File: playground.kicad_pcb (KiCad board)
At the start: 4 copper layers, 80 x 51 mm, 74 parts, among them IC1 TXU0101DBVR, IC11 LM3940IMP-3.3_NOPB, IC2 TXU0101DBVR, IC3 TXU0101DBVR, IC4 TXU0101DBVR, IC5 TXU0101DBVR, IC6 TXU0101DBVR, IC7 TXU0101DBVR, IC8 TXU0101DBVR, IC9 L293DD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

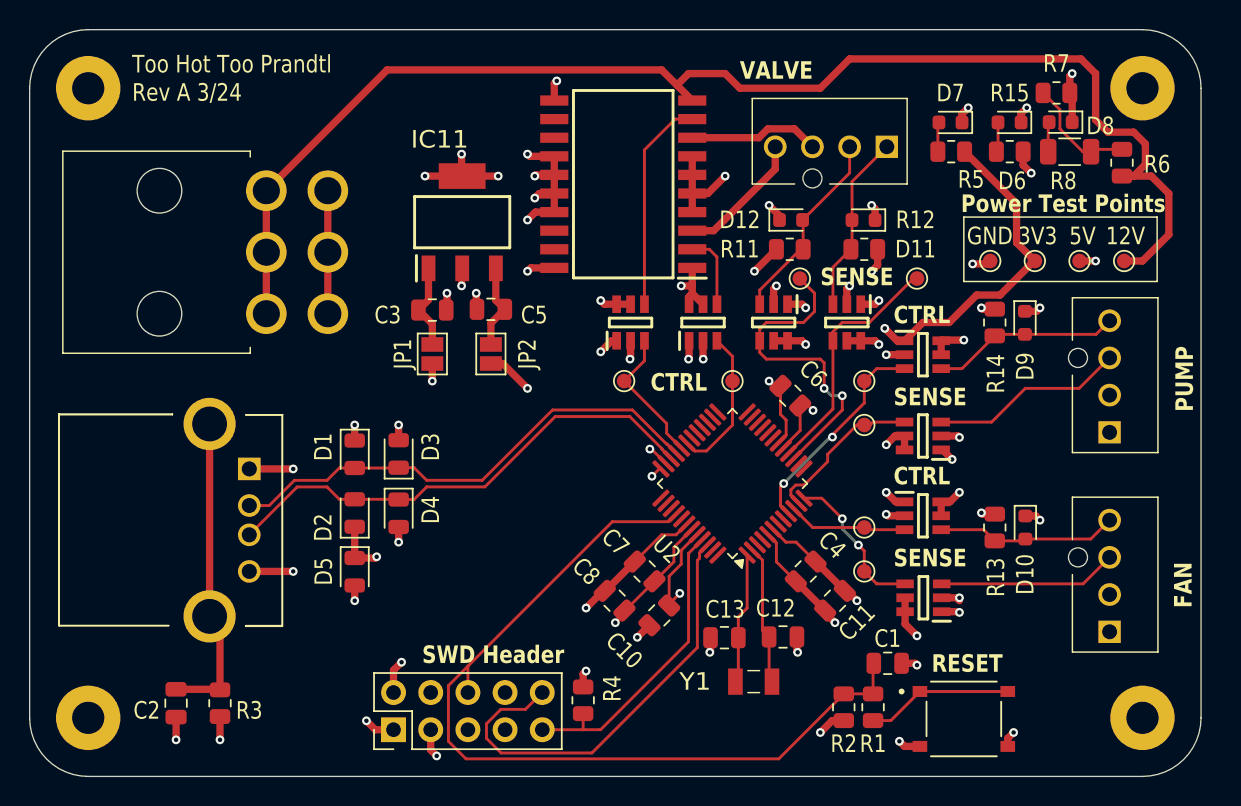
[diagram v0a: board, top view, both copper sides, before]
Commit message: Small part substitutions. Working on BOM
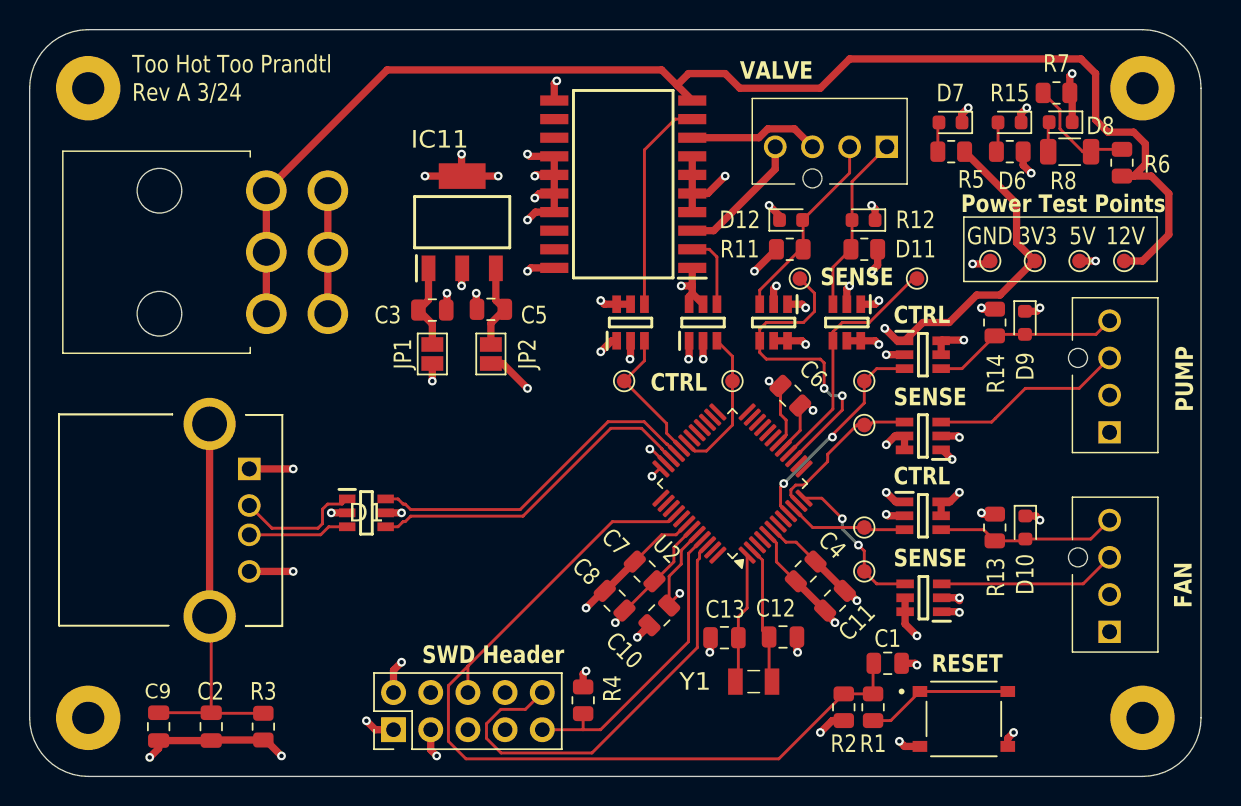
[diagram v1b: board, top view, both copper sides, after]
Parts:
- removed D2: D_Zener, Diode_SMD:D_0805_2012Metric
- removed D3, D4, D5: ~, Diode_SMD:D_0805_2012Metric
- added C9: 2.2n, Capacitor_SMD:C_0805_2012Metric, F.Cu at (90.8, 106.6)
- C2: value 4.5nF -> 2.2n
- C3: value 4.7n -> 470n
- D1: value ~ -> IP4234CZ6,125; footprint Diode_SMD:D_0805_2012Metric -> custom_footprints:SOP95P275X110-6N
- moved D1 4.08 mm to (105.0, 92.0), turned to 0 degrees
- moved R3 3.36 mm to (98.0, 106.6)
- moved C2 2.88 mm to (94.4, 106.6)
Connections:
- D1 pad 1: +5V -> /IN_USB_D-
- D1 pad 2: /USB_D- -> GND
- J1 pad 2: /USB_D- -> /IN_USB_D-
- J1 pad 3: /USB_D+ -> /IN_USB_D+
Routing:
- net /USB_D+: track 34.1 -> 23.2 mm
- net /USB_D-: track 33.9 -> 23.5 mm
- net /IN_USB_D-: track 0.00 -> 8.74 mm
- net /IN_USB_D+: track 0.00 -> 6.92 mm
- net /usb_shield_gnd: track 21.5 -> 28.2 mm
- net GND: track 97.9 -> 103.0 mm, vias 45 -> 43
- net +5V: track 37.1 -> 33.5 mm, vias 20 -> 19

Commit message: Added all part numbers
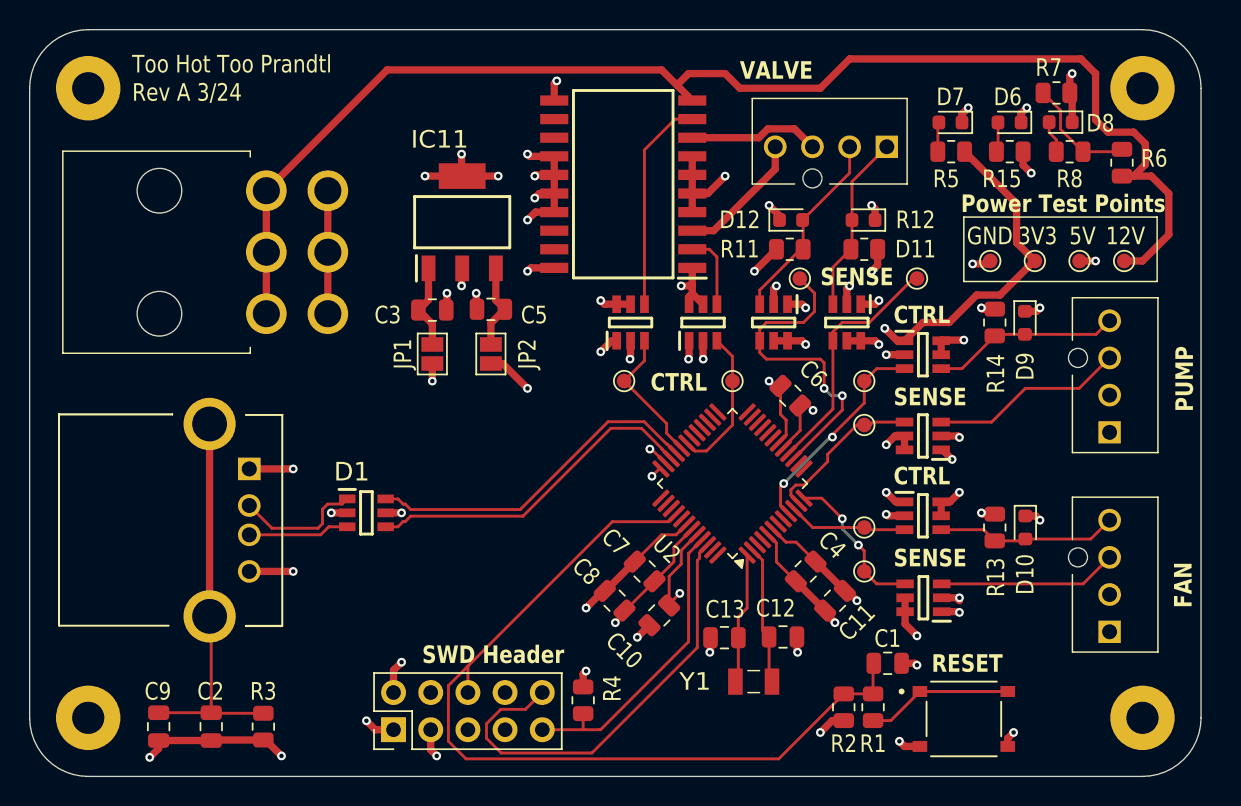
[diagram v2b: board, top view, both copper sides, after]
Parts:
- R11, R12, R13, R14, R15: value 20R -> 200R
- R8: footprint Resistor_SMD:R_1206_3216Metric -> Resistor_SMD:R_0805_2012Metric

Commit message: Version exported for production.
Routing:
- net +12V: track 93.2 -> 49.8 mm
- net GND: track 103.0 -> 94.6 mm
- added copper zone on F.Cu, net +12V
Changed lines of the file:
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@@
 	)
 	(segment
-		(start 117.828 63.84)
-		(end 117.828 62.672)
-		(width 0.5)
-		(layer "F.Cu")
-		(net 4)
-	)
-	(segment
 		(start 147.0875 92.0875)
 		(end 147 92)
@@
 	)
 	(segment
+		(start 117.788 63.8)
+		(end 117.828 63.84)
+		(width 0.5)
+		(layer "F.Cu")
+		(net 4)
+	)
+	(segment
 		(start 138.759466 77.75)
 		(end 139.75 77.75)
@@
 	)
 	(segment
-		(start 117.828 62.672)
-		(end 118 62.5)
-		(width 0.5)
-		(layer "F.Cu")
-		(net 4)
-	)
-	(segment
 		(start 133 74)
 		(end 131.5 75.5)
@@
 	)
 	(segment
+		(start 116 63.8)
+		(end 117.788 63.8)
+		(width 0.5)
+		(layer "F.Cu")
+		(net 4)
+	)
+	(segment
 		(start 144.25 87.7)
 		(end 144.35 87.7)
@@
 	)
 	(via
-		(at 118 62.5)
+		(at 116 63.8)
 		(size 0.6)
 		(drill 0.3)
@@
 	)
 	(segment
-		(start 102.364999 78.399999)
-		(end 102.365 74.199999)
-		(width 0.5)
-		(layer "F.Cu")
-		(net 5)
-	)
-	(segment
 		(start 127.252 70.19)
 		(end 128.31 70.19)
@@
 	)
 	(segment
-		(start 102.365 70)
-		(end 102.365 74.199999)
-		(width 0.5)
-		(layer "F.Cu")
-		(net 5)
-	)
-	(segment
 		(start 145.4 86.75)
 		(end 145.5 86.85)
@@
 	)
 	(segment
-		(start 138 61)
-		(end 153.8 61)
-		(width 0.5)
-		(layer "F.Cu")
-		(net 55)
-	)
-	(segment
-		(start 158.2 66.8)
-		(end 158.2 68.2)
-		(width 0.5)
-		(layer "F.Cu")
-		(net 55)
-	)
-	(segment
-		(start 125.162 61.75)
-		(end 126.206 62.794)
-		(width 0.5)
-		(layer "F.Cu")
-		(net 55)
-	)
-	(segment
-		(start 157.4 69)
-		(end 156.6 69)
-		(width 0.5)
-		(layer "F.Cu")
-		(net 55)
-	)
-	(segment
-		(start 154.8 65.159378)
-		(end 155.640622 66)
-		(width 0.5)
-		(layer "F.Cu")
-		(net 55)
-	)
-	(segment
-		(start 126.206 62.794)
-		(end 127.252 63.84)
-		(width 0.5)
-		(layer "F.Cu")
-		(net 55)
-	)
-	(segment
 		(start 159.8 73)
 		(end 159.8 70.2)
@@
 	)
 	(segment
-		(start 153.8 61)
-		(end 154.8 62)
-		(width 0.5)
-		(layer "F.Cu")
-		(net 55)
-	)
-	(segment
-		(start 158.2 68.2)
-		(end 157.4 69)
-		(width 0.5)
-		(layer "F.Cu")
-		(net 55)
-	)
-	(segment
-		(start 129.5 62)
-		(end 130.5 63)
-		(width 0.5)
-		(layer "F.Cu")
-		(net 55)
-	)
-	(segment
-		(start 154.8 62)
-		(end 154.8 65.159378)
-		(width 0.5)
-		(layer "F.Cu")
-		(net 55)
-	)
-	(segment
 		(start 156.75 74.8)
 		(end 158 74.8)
@@
 	)
 	(segment
-		(start 136 63)
-		(end 138 61)
-		(width 0.5)
-		(layer "F.Cu")
-		(net 55)
-	)
-	(segment
-		(start 127 62)
-		(end 129.5 62)
-		(width 0.5)
-		(layer "F.Cu")
-		(net 55)
-	)
-	(segment
-		(start 130.5 63)
-		(end 136 63)
+		(start 154.6 61.2)
+		(end 153.8 60.4)
 		(width 0.5)
 		(layer "F.Cu")
@@
 	)
 	(segment
-		(start 155.640622 66)
-		(end 157.4 66)
+		(start 155 66)
+		(end 154.6 65.6)
 		(width 0.5)
 		(layer "F.Cu")
@@
 	)
 	(segment
-		(start 157.4 66)
-		(end 158.2 66.8)
+		(start 157.8 66)
+		(end 155 66)
 		(width 0.5)
 		(layer "F.Cu")
@@
 	)
 	(segment
-		(start 98.165 69.999999)
-		(end 98.165 74.2)
+		(start 128.8 60.4)
+		(end 127.2 62)
 		(width 0.5)
 		(layer "F.Cu")
@@
 	)
 	(segment
-		(start 98.165 69.999999)
-		(end 106.414999 61.75)
+		(start 154.6 65.6)
+		(end 154.6 61.2)
 		(width 0.5)
 		(layer "F.Cu")
@@
 	)
 	(segment
-		(start 98.165 78.399999)
-		(end 98.165 74.2)
+		(start 158.6 69)
+		(end 158.6 66.8)
 		(width 0.5)
 		(layer "F.Cu")
@@
 	)
 	(segment
-		(start 126.206 62.794)
-		(end 127 62)
+		(start 153.8 60.4)
+		(end 128.8 60.4)
 		(width 0.5)
 		(layer "F.Cu")
@@
 	)
 	(segment
-		(start 106.414999 61.75)
-		(end 125.162 61.75)
+		(start 158.6 66.8)
+		(end 157.8 66)
 		(width 0.5)
 		(layer "F.Cu")
@@
 	)
 	(zone
+		(net 55)
+		(net_name "+12V")
+		(layer "F.Cu")
+		(hatch edge 0.5)
+		(priority 3)
+		(connect_pads yes
+			(clearance 0.5)
+		)
+		(min_thickness 0.25)
+		(filled_areas_thickness no)
+		(fill yes
+			(thermal_gap 0.5)
+			(thermal_bridge_width 0.5)
+		)
+		(polygon
+			(pts
+				(xy 100.2 68) (xy 100.2 80.2) (xy 96 80.2) (xy 96 68) (xy 101.6 62.4) (xy 105.6 62.4) (xy 108 60)
+				(xy 126 60) (xy 128.6 62.517782) (xy 128.6 64.4) (xy 125.8 64.4) (xy 123.4 62) (xy 109 62) (xy 107 64)
+				(xy 104.2 64)
+			)
+		)
+	)
+	(zone
